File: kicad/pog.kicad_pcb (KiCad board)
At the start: 2 copper layers, 304.2 x 115.2 mm, 196 parts, among them J1 USB_C_Receptacle, U1 ATmega32U4-A

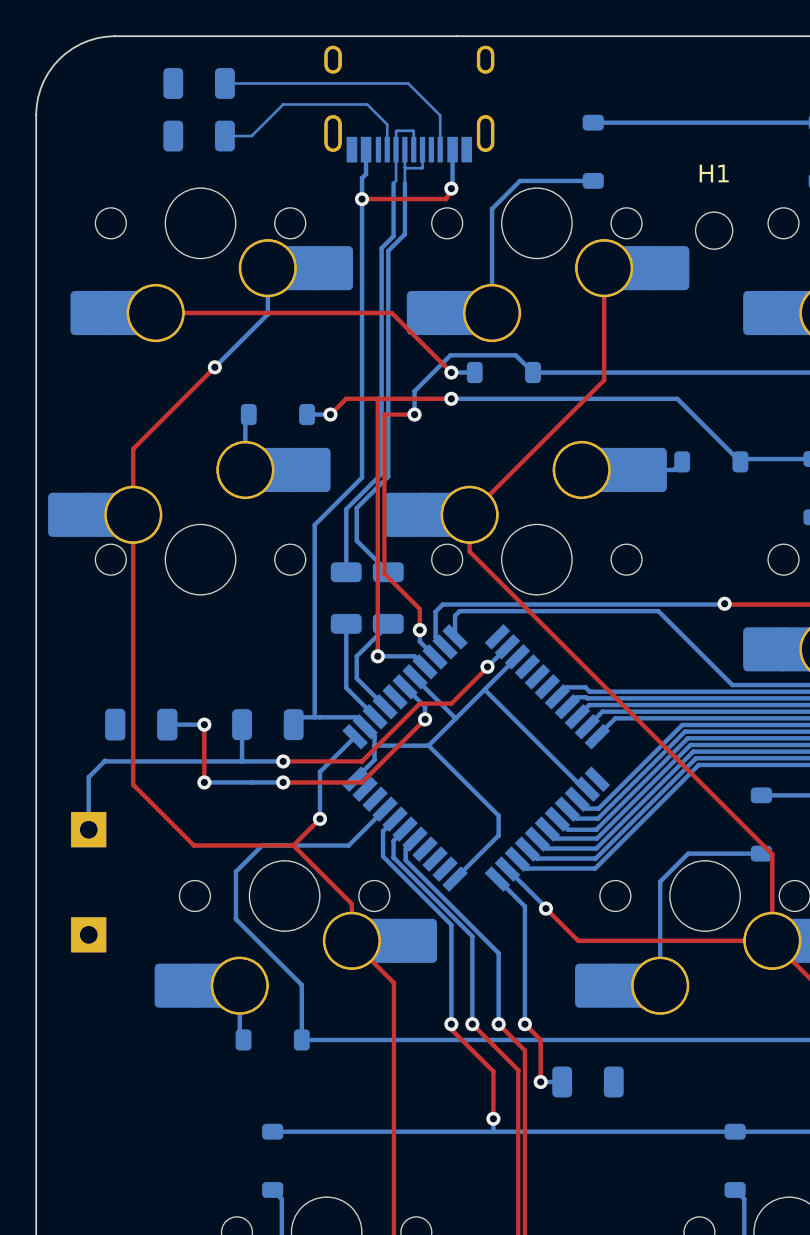
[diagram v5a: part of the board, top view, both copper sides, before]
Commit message: add grounding plane
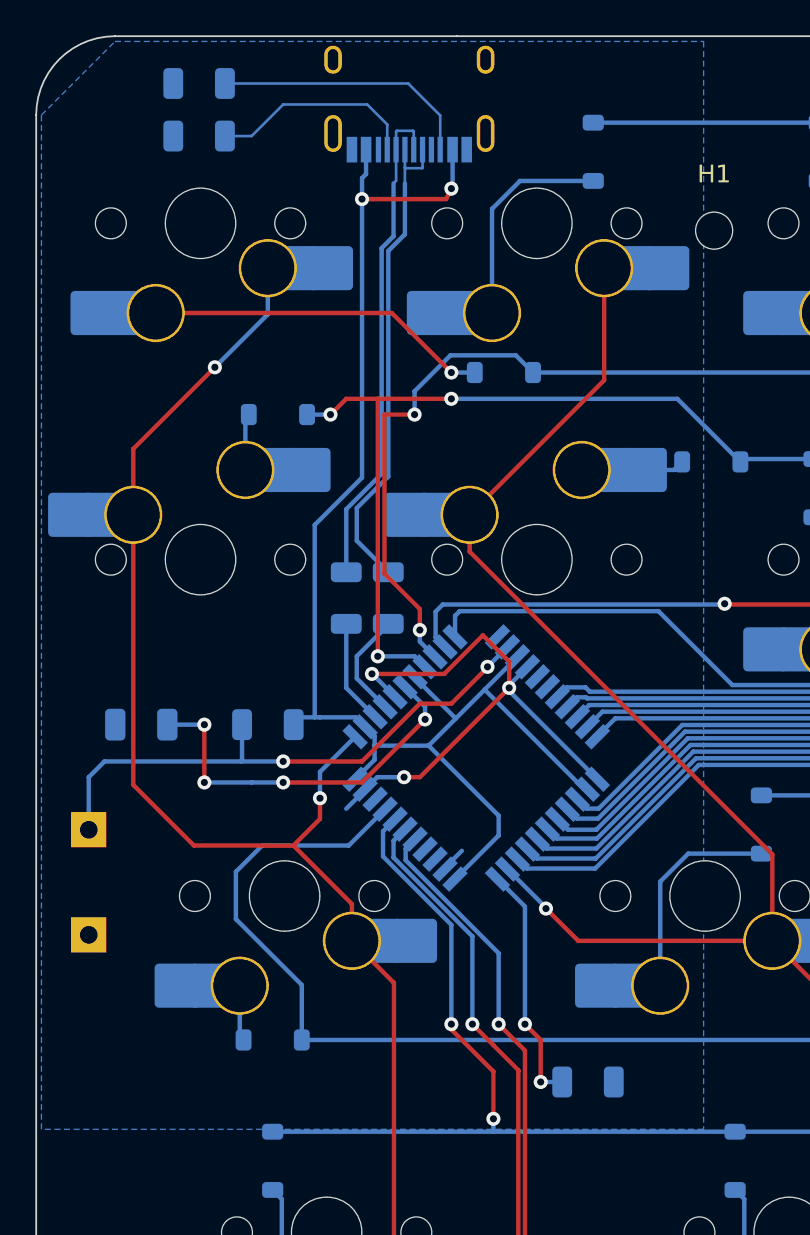
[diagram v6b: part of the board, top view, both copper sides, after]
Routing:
- net GND: track 0.00 -> 35.2 mm, vias 0 -> 3
- added copper zone on B.Cu, net GND
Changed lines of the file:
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@@
     (fp_arc (start -5.499999 15.28125) (mid -5.853552 15.134803) (end -5.999999 14.78125)
       (stroke (width 0.05) (type solid)) (layer "Eco2.User"))
-    (fp_arc (start 7.500001 -15.28125) (mid 7.853571 -15.134806) (end 8.000001 -14.78125)
+    (fp_arc (start 7.500001 -15.28125) (mid 7.853536 -15.1348) (end 8.000001 -14.78125)
       (stroke (width 0.05) (type solid)) (layer "Eco2.User"))
-    (fp_arc (start 7.500001 8.53125) (mid 7.853571 8.677694) (end 8.000001 9.03125)
+    (fp_arc (start 7.500001 8.53125) (mid 7.853536 8.6777) (end 8.000001 9.03125)
       (stroke (width 0.05) (type solid)) (layer "Eco2.User"))
     (fp_arc (start 8.000001 -9.03125) (mid 7.853554 -8.677696) (end 7.500001 -8.53125)
@@
     (fp_arc (start 8.53125 -5.499999) (mid 8.677685 -5.853565) (end 9.03125 -5.999999)
       (stroke (width 0.05) (type solid)) (layer "Eco2.User"))
-    (fp_arc (start 9.03125 8.000001) (mid 8.677729 7.853537) (end 8.53125 7.500001)
+    (fp_arc (start 9.03125 8.000001) (mid 8.677693 7.853543) (end 8.53125 7.500001)
       (stroke (width 0.05) (type solid)) (layer "Eco2.User"))
-    (fp_arc (start 14.780039 -5.999999) (mid 15.133567 -5.853539) (end 15.280039 -5.499999)
+    (fp_arc (start 14.780039 -5.999999) (mid 15.133602 -5.853545) (end 15.280039 -5.499999)
       (stroke (width 0.05) (type solid)) (layer "Eco2.User"))
-    (fp_arc (start 15.28125 7.500001) (mid 15.134806 7.853571) (end 14.78125 8.000001)
+    (fp_arc (start 15.28125 7.500001) (mid 15.1348 7.853536) (end 14.78125 8.000001)
       (stroke (width 0.05) (type solid)) (layer "Eco2.User"))
     (pad "" thru_hole circle (at -11.90625 -6.985 180) (size 4 4) (drill 3.048) (layers "*.Cu" "B.Mask"))
@@
   (segment (start 42.287732 71.47792) (end 42.287732 88.14792) (width 0.25) (layer "F.Cu") (net 88))
   (segment (start 36.593983 63.698384) (end 39.907732 67.012133) (width 0.25) (layer "F.Cu") (net 88))
-  (segment (start 27.525232 44.96792) (end 27.525232 41.233304) (width 0.25) (layer "F.Cu") (net 88))
   (segment (start 38.099968 62.192399) (end 36.593983 63.698384) (width 0.25) (layer "F.Cu") (net 88))
+  (segment (start 27.525232 44.96792) (end 27.525232 41.233304) (width 0.25) (layer "F.Cu") (net 88))
+  (segment (start 38.099968 61.01948) (end 38.099968 62.192399) (width 0.25) (layer "F.Cu") (net 88))
   (segment (start 37.524732 126.24792) (end 37.524732 107.19792) (width 0.25) (layer "F.Cu") (net 88))
   (segment (start 37.540732 107.18192) (end 37.540732 92.89492) (width 0.25) (layer "F.Cu") (net 88))
@@
   (segment (start 37.540732 92.89492) (end 42.287732 88.14792) (width 0.25) (layer "F.Cu") (net 88))
   (via (at 32.146848 36.611688) (size 0.8) (drill 0.4) (layers "F.Cu" "B.Cu") (net 88))
-  (via (at 38.099968 62.192399) (size 0.8) (drill 0.4) (layers "F.Cu" "B.Cu") (net 88))
+  (via (at 38.099968 61.01948) (size 0.8) (drill 0.4) (layers "F.Cu" "B.Cu") (net 88))
   (segment (start 32.146848 36.611688) (end 35.145232 33.613304) (width 0.25) (layer "B.Cu") (net 88))
-  (segment (start 38.099968 62.192399) (end 38.099968 59.5312) (width 0.25) (layer "B.Cu") (net 88))
-  (segment (start 38.099968 59.5312) (end 40.09329 57.537878) (width 0.25) (layer "B.Cu") (net 88))
   (segment (start 35.145232 33.613304) (end 35.145232 30.99792) (width 0.25) (layer "B.Cu") (net 88))
+  (segment (start 38.099968 59.5312) (end 40.09329 57.537878) (width 0.25) (layer "B.Cu") (net 88))
+  (segment (start 38.099968 61.01948) (end 38.099968 59.5312) (width 0.25) (layer "B.Cu") (net 88))
   (segment (start 52.72684 69.09792) (end 50.899176 67.270256) (width 0.25) (layer "F.Cu") (net 89))
   (segment (start 63.720232 69.09792) (end 63.720232 64.198707) (width 0.25) (layer "F.Cu") (net 89))
@@
   (segment (start 51.54842 62.204783) (end 52.149053 62.805416) (width 0.25) (layer "B.Cu") (net 103))
   (segment (start 53.751428 62.805416) (end 58.930828 57.626016) (width 0.25) (layer "B.Cu") (net 103))
+  (segment (start 47.327304 51.792144) (end 48.815584 53.280424) (width 0.25) (layer "F.Cu") (net 104))
+  (segment (start 48.815584 54.768704) (end 43.755432 59.828856) (width 0.25) (layer "F.Cu") (net 104))
+  (segment (start 43.755432 59.828856) (end 42.862464 59.828856) (width 0.25) (layer "F.Cu") (net 104))
+  (segment (start 45.141034 53.978414) (end 47.327304 51.792144) (width 0.25) (layer "F.Cu") (net 104))
+  (segment (start 41.042302 53.978414) (end 45.141034 53.978414) (width 0.25) (layer "F.Cu") (net 104))
+  (segment (start 48.815584 53.280424) (end 48.815584 54.768704) (width 0.25) (layer "F.Cu") (net 104))
+  (via (at 42.862464 59.828856) (size 0.8) (drill 0.4) (layers "F.Cu" "B.Cu") (net 104))
+  (via (at 48.815584 54.768704) (size 0.8) (drill 0.4) (layers "F.Cu" "B.Cu") (net 104))
+  (via (at 41.042302 53.978414) (size 0.8) (drill 0.4) (layers "F.Cu" "B.Cu") (net 104))
+  (segment (start 48.649282 54.780162) (end 53.811162 59.942042) (width 0.25) (layer "B.Cu") (net 104))
+  (segment (start 40.658976 60.507727) (end 40.658976 60.544064) (width 0.25) (layer "B.Cu") (net 104))
+  (segment (start 42.862464 59.828856) (end 41.337847 59.828856) (width 0.25) (layer "B.Cu") (net 104))
+  (segment (start 41.059309 53.978414) (end 42.356032 55.275137) (width 0.25) (layer "B.Cu") (net 104))
+  (segment (start 49.851364 53.57808) (end 48.815584 54.61386) (width 0.25) (layer "B.Cu") (net 104))
+  (segment (start 41.042302 53.978414) (end 41.059309 53.978414) (width 0.25) (layer "B.Cu") (net 104))
+  (segment (start 41.337847 59.828856) (end 40.658976 60.507727) (width 0.25) (layer "B.Cu") (net 104))
+  (segment (start 40.658976 60.544064) (end 39.588248 61.614792) (width 0.25) (layer "B.Cu") (net 104))
+  (segment (start 48.815584 54.61386) (end 48.815584 54.768704) (width 0.25) (layer "B.Cu") (net 104))
+  (segment (start 45.184459 64.948261) (end 46.13668 63.99604) (width 0.25) (layer "B.Cu") (net 104))
+  (segment (start 48.815584 54.768704) (end 48.66074 54.768704) (width 0.25) (layer "B.Cu") (net 104))
+  (segment (start 45.184459 65.03321) (end 45.184459 64.948261) (width 0.25) (layer "B.Cu") (net 104))
+  (segment (start 48.66074 54.768704) (end 48.649282 54.780162) (width 0.25) (layer "B.Cu") (net 104))
   (segment (start 31.551536 60.126512) (end 31.551536 56.852296) (width 0.25) (layer "F.Cu") (net 105))
   (segment (start 44.053088 56.55464) (end 40.481216 60.126512) (width 0.25) (layer "F.Cu") (net 105))
@@
   (segment (start 33.686688 58.884328) (end 33.635128 58.935888) (width 0.25) (layer "B.Cu") (net 122))
   (segment (start 47.588623 53.57808) (end 48.719993 52.44671) (width 0.25) (layer "B.Cu") (net 122))
-  (segment (start 25.947632 58.884328) (end 25.896072 58.935888) (width 0.25) (layer "B.Cu") (net 122))
   (segment (start 25.896072 58.935888) (end 25.003104 59.828856) (width 0.25) (layer "B.Cu") (net 122))
   (segment (start 33.635128 58.935888) (end 25.896072 58.935888) (width 0.25) (layer "B.Cu") (net 122))
@@
   (segment (start 51.817924 77.092904) (end 50.60152 77.092904) (width 0.25) (layer "B.Cu") (net 123))
   (segment (start 49.708552 73.818688) (end 49.708552 67.15314) (width 0.25) (layer "B.Cu") (net 123))
+  (zone (net 104) (net_name "GND") (layer "B.Cu") (hatch edge 0.5)
+    (connect_pads (clearance 0.5))
+    (min_thickness 0.25) (filled_areas_thickness no)
+    (fill yes (thermal_gap 0.5) (thermal_bridge_width 0.5))
+    (polygon
+      (pts
+        (xy 22.3242 22.3242)
+        (xy 26.491384 18.157016)
+        (xy 59.828856 18.157016)
+        (xy 59.828856 79.771808)
+        (xy 22.3242 79.771808)
+      )
+    )
+  )
 )

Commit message: finished keyboard
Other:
- board text added: "Designed by Axel Kappel"

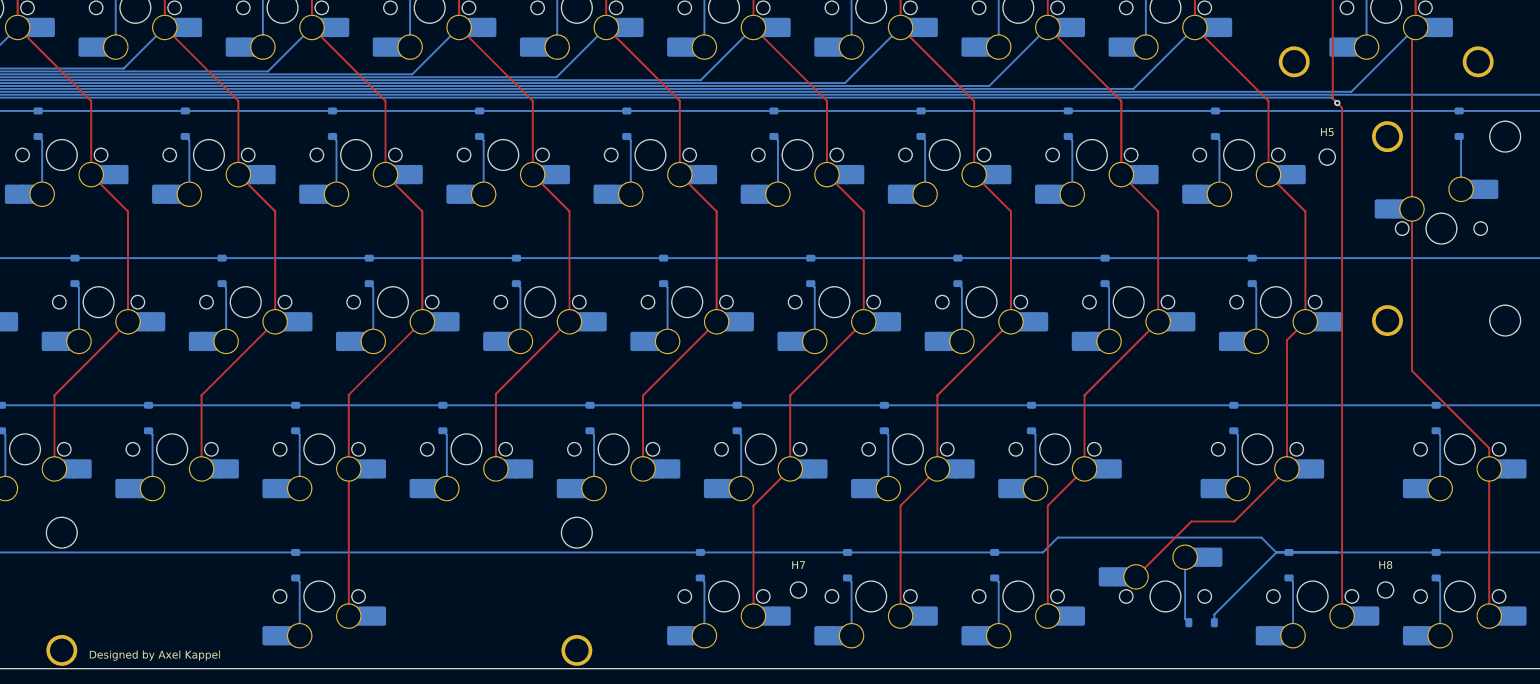
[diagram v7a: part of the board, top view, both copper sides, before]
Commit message: switch to pcb mount stabilizers
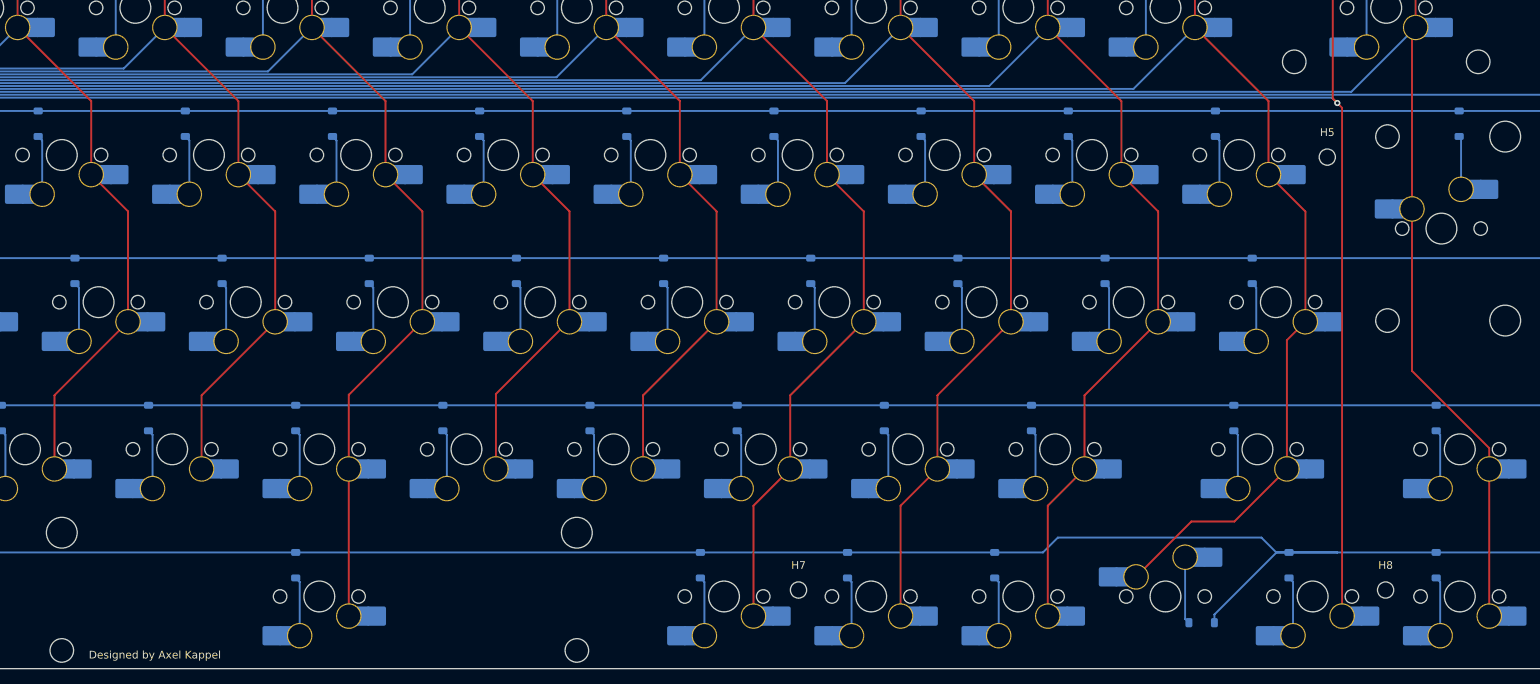
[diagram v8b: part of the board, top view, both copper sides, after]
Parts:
- S1: footprint PCM_marbastlib-mx:STAB_MX_P_2u -> PCM_marbastlib-mx:STAB_MX_2u
- S2: footprint PCM_marbastlib-mx:STAB_MX_P_ISO -> PCM_marbastlib-mx:STAB_MX_ISO
- S3: footprint PCM_marbastlib-mx:STAB_MX_P_4.5u -> PCM_marbastlib-mx:STAB_MX_4.5u
